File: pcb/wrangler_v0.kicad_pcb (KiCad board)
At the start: 4 copper layers, 39.7 x 20.8 mm, 60 parts, among them J1 HDMI_A, J2 USB_B_Micro, J3 Conn_01x10, J4 Conn_01x10, SW1 SW_Push, SW2 SW_Push, U1 ICE40UP5K-SG48ITR, U2 W25Q32JVSSIM, U3 AP2127K-3.3, U4 AP2127K-1.2

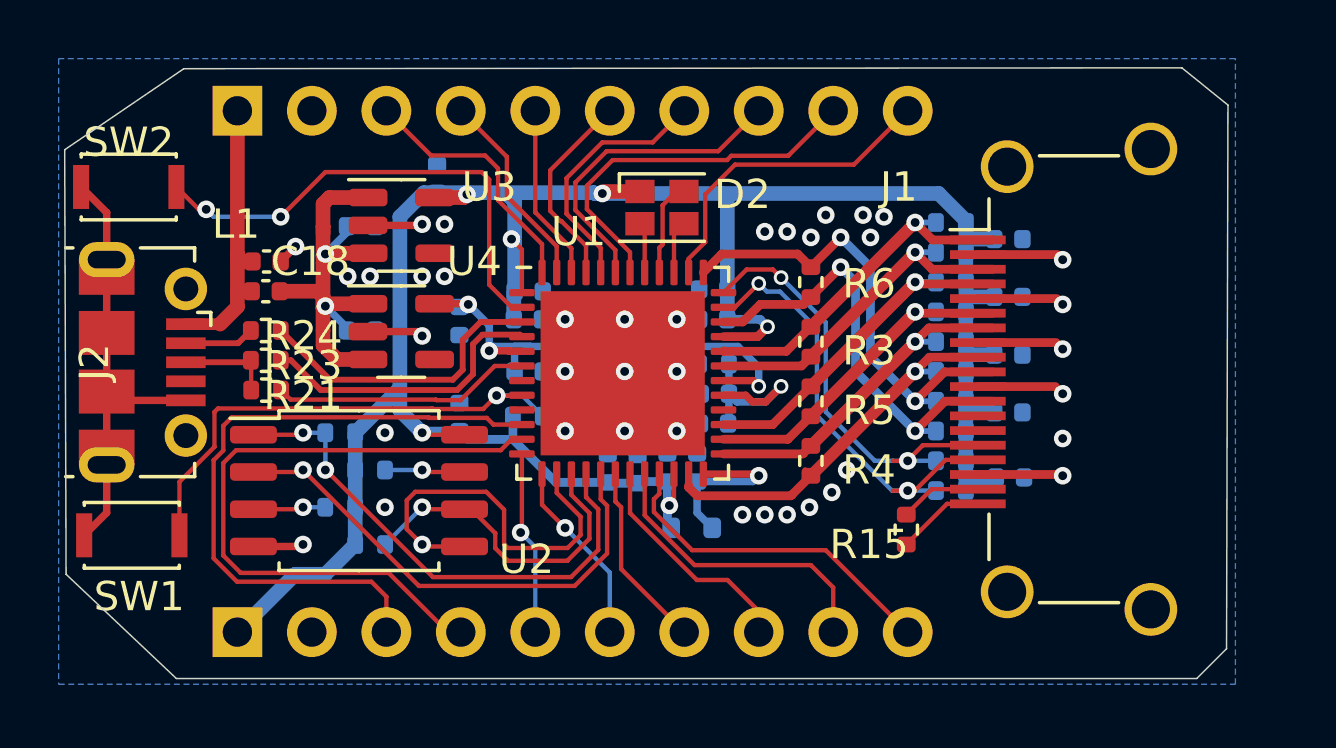
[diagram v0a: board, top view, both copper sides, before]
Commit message: updated with comments from revspace and matt
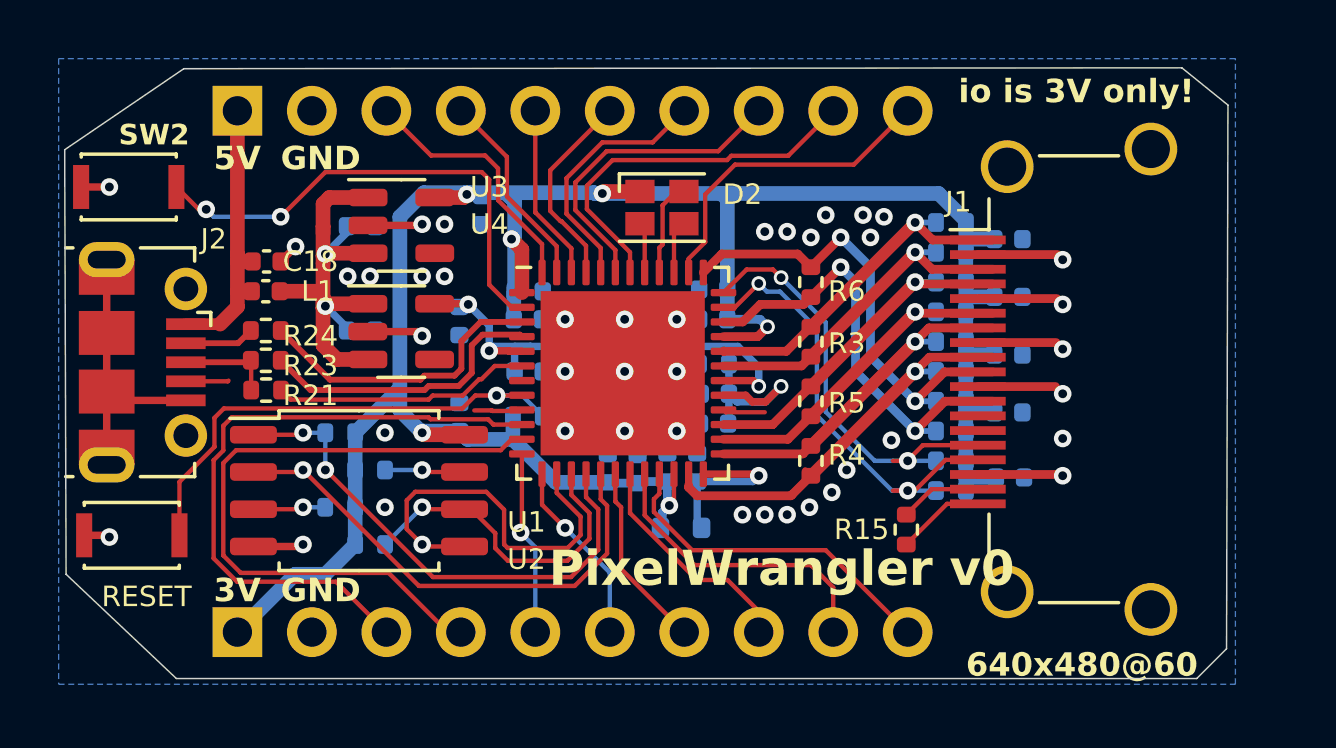
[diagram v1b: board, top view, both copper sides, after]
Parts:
- moved C21 1.86 mm to (123.8, 96.1), turned to -90 degrees
- moved D1 0.36 mm to (130.6, 106.9)
- renumbered SW1 to RESET
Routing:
- net GND: track 36.4 -> 32.7 mm, vias 39 -> 42
- net /IOB_16A: track 0.00 -> 1.65 mm
- net unconnected-(J2-ID-Pad4): track 0.00 -> 1.47 mm
- net /IOT_41A: track 0.00 -> 1.44 mm
- net /IOB_18A: track 22.7 -> 22.0 mm
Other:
- board text added: "3V"
- board text added: "5V"
- board text added: "640x480@60"
- board text added: "GND"
- board text added: "PixelWrangler v0"
- board text added: "io is 3V only!"

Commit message: pcb: added CDONE pullup resistor and some silkscreen tweaks
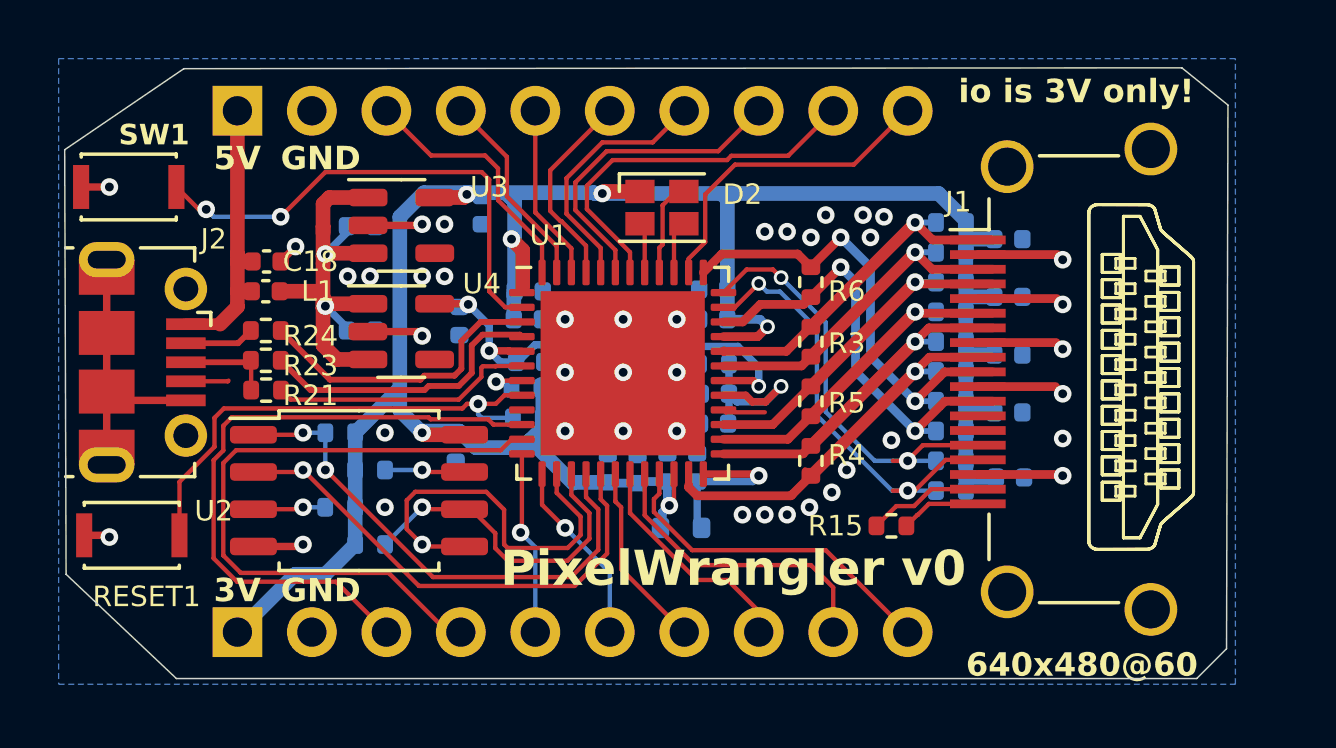
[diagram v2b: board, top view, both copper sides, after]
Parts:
- added R25: 2.2k, Resistor_SMD:R_0402_1005Metric, B.Cu at (125.3, 102.2)
- moved C13 1.05 mm to (122.9, 104.2), turned to -90 degrees
- moved R15 0.52 mm to (137.7, 106.9), turned to 0 degrees
- moved C1 0.33 mm to (125.4, 101.3)
- moved R1 0.06 mm to (125.3, 103.2), turned to 0 degrees
- renumbered RESET to RESET1, SW2 to SW1
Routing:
- net /IOB_16A: track 1.65 -> 0.05 mm
- net +3.3V: track 84.0 -> 85.4 mm
- net /HDMI_5v: track 2.80 -> 3.98 mm
- net /CDONE: track 0.00 -> 1.13 mm, vias 0 -> 1
- net +1V2: track 17.4 -> 16.4 mm
